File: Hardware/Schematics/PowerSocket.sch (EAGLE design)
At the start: 73 parts, among them T1 BT138-H, T2 BT138-H, T3 BT138-H, T4 BT138-H, T5 BT138-H, T6 BT138-H

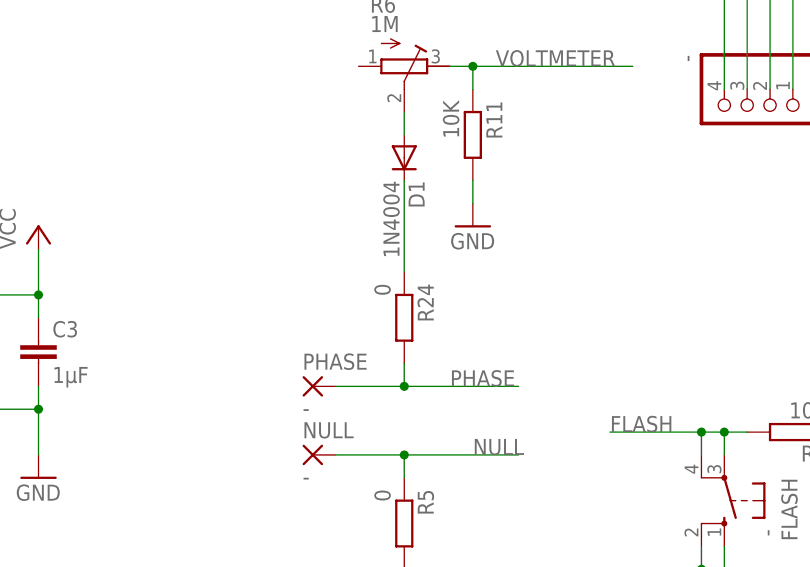
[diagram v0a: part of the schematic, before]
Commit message: Changed package for triac.
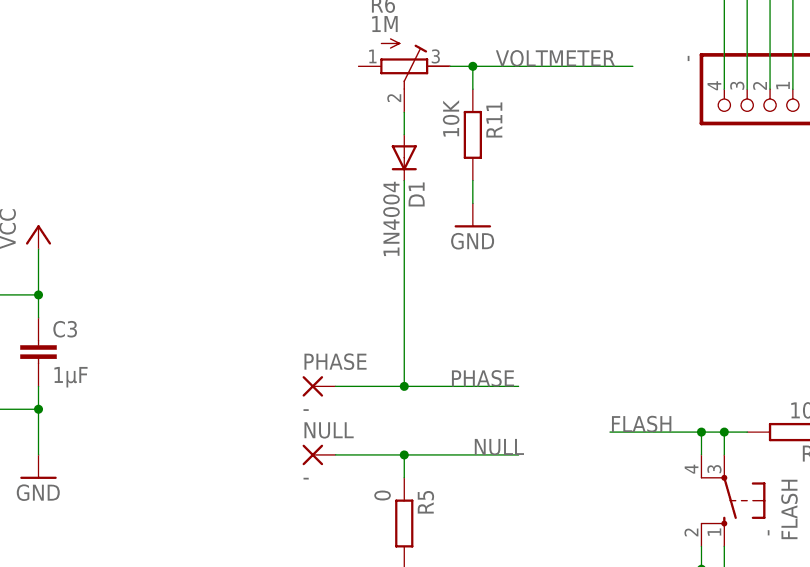
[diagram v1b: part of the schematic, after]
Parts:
- removed R24: 0, eagle-ltspice:RR2010
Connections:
- removed net N$41: D1.C, R24.1
- net PHASE: now also D1.C; no longer R24.2
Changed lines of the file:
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@@
 <grid distance="0.1" unitdist="inch" unit="inch" style="lines" multiple="1" display="no" altdistance="0.01" altunitdist="inch" altunit="inch"/>
 <layers>
-<layer number="1" name="Top" color="4" fill="1" visible="yes" active="no"/>
-<layer number="16" name="Bottom" color="1" fill="1" visible="yes" active="no"/>
-<layer number="17" name="Pads" color="2" fill="1" visible="yes" active="no"/>
-<layer number="18" name="Vias" color="2" fill="1" visible="yes" active="no"/>
-<layer number="19" name="Unrouted" color="6" fill="1" visible="yes" active="no"/>
-<layer number="20" name="Dimension" color="15" fill="1" visible="yes" active="no"/>
-<layer number="21" name="tPlace" color="7" fill="1" visible="yes" active="no"/>
-<layer number="22" name="bPlace" color="7" fill="1" visible="yes" active="no"/>
-<layer number="23" name="tOrigins" color="15" fill="1" visible="yes" active="no"/>
-<layer number="24" name="bOrigins" color="15" fill="1" visible="yes" active="no"/>
-<layer number="25" name="tNames" color="7" fill="1" visible="yes" active="no"/>
-<layer number="26" name="bNames" color="7" fill="1" visible="yes" active="no"/>
-<layer number="27" name="tValues" color="7" fill="1" visible="yes" active="no"/>
-<layer number="28" name="bValues" color="7" fill="1" visible="yes" active="no"/>
+<layer number="1" name="Top" color="4" fill="1" visible="no" active="no"/>
+<layer number="16" name="Bottom" color="1" fill="1" visible="no" active="no"/>
+<layer number="17" name="Pads" color="2" fill="1" visible="no" active="no"/>
+<layer number="18" name="Vias" color="2" fill="1" visible="no" active="no"/>
+<layer number="19" name="Unrouted" color="6" fill="1" visible="no" active="no"/>
+<layer number="20" name="Dimension" color="15" fill="1" visible="no" active="no"/>
+<layer number="21" name="tPlace" color="7" fill="1" visible="no" active="no"/>
+<layer number="22" name="bPlace" color="7" fill="1" visible="no" active="no"/>
+<layer number="23" name="tOrigins" color="15" fill="1" visible="no" active="no"/>
+<layer number="24" name="bOrigins" color="15" fill="1" visible="no" active="no"/>
+<layer number="25" name="tNames" color="7" fill="1" visible="no" active="no"/>
+<layer number="26" name="bNames" color="7" fill="1" visible="no" active="no"/>
+<layer number="27" name="tValues" color="7" fill="1" visible="no" active="no"/>
+<layer number="28" name="bValues" color="7" fill="1" visible="no" active="no"/>
 <layer number="29" name="tStop" color="7" fill="3" visible="no" active="no"/>
 <layer number="30" name="bStop" color="7" fill="6" visible="no" active="no"/>
@@
 <layer number="35" name="tGlue" color="7" fill="4" visible="no" active="no"/>
 <layer number="36" name="bGlue" color="7" fill="5" visible="no" active="no"/>
-<layer number="37" name="tTest" color="7" fill="1" visible="yes" active="no"/>
-<layer number="38" name="bTest" color="7" fill="1" visible="yes" active="no"/>
+<layer number="37" name="tTest" color="7" fill="1" visible="no" active="no"/>
+<layer number="38" name="bTest" color="7" fill="1" visible="no" active="no"/>
 <layer number="39" name="tKeepout" color="4" fill="11" visible="no" active="no"/>
 <layer number="40" name="bKeepout" color="1" fill="11" visible="no" active="no"/>
@@
 <layer number="44" name="Drills" color="7" fill="1" visible="no" active="no"/>
 <layer number="45" name="Holes" color="7" fill="1" visible="no" active="no"/>
-<layer number="46" name="Milling" color="3" fill="1" visible="yes" active="no"/>
-<layer number="47" name="Measures" color="7" fill="1" visible="yes" active="no"/>
-<layer number="48" name="Document" color="7" fill="1" visible="yes" active="no"/>
-<layer number="49" name="Reference" color="7" fill="1" visible="yes" active="no"/>
-<layer number="50" name="dxf" color="7" fill="1" visible="yes" active="no"/>
-<layer number="51" name="tDocu" color="7" fill="1" visible="yes" active="no"/>
-<layer number="52" name="bDocu" color="7" fill="1" visible="yes" active="no"/>
-<layer number="56" name="wert" color="7" fill="1" visible="yes" active="no"/>
+<layer number="46" name="Milling" color="3" fill="1" visible="no" active="no"/>
+<layer number="47" name="Measures" color="7" fill="1" visible="no" active="no"/>
+<layer number="48" name="Document" color="7" fill="1" visible="no" active="no"/>
+<layer number="49" name="Reference" color="7" fill="1" visible="no" active="no"/>
+<layer number="50" name="dxf" color="7" fill="1" visible="no" active="no"/>
+<layer number="51" name="tDocu" color="7" fill="1" visible="no" active="no"/>
+<layer number="52" name="bDocu" color="7" fill="1" visible="no" active="no"/>
+<layer number="56" name="wert" color="7" fill="1" visible="no" active="no"/>
 <layer number="90" name="Modules" color="5" fill="1" visible="yes" active="yes"/>
 <layer number="91" name="Nets" color="2" fill="1" visible="yes" active="yes"/>
@@
 <part name="R14" library="rcl" deviceset="R-EU_" device="R0805" value="150"/>
 <part name="R18" library="rcl" deviceset="R-EU_" device="R0805" value="150"/>
-<part name="R24" library="eagle-ltspice" deviceset="R" device="R2010" value="0"/>
 <part name="T1" library="triac" deviceset="BT138" device="-H"/>
 <part name="T2" library="triac" deviceset="BT138" device="-H"/>
@@
 <instance part="R14" gate="G$1" x="-152.4" y="144.78" rot="R90"/>
 <instance part="R18" gate="G$1" x="-152.4" y="55.88" rot="R270"/>
-<instance part="R24" gate="G$1" x="-35.56" y="-27.94" rot="R270"/>
 <instance part="T1" gate="G$1" x="-152.4" y="193.04" rot="R270"/>
 <instance part="T2" gate="G$1" x="-127" y="193.04" rot="R270"/>
@@
 <wire x1="-43.18" y1="-35.56" x2="-35.56" y2="-35.56" width="0.1524" layer="91"/>
 <label x="-30.48" y="-35.56" size="1.778" layer="95"/>
-<pinref part="R24" gate="G$1" pin="2"/>
 <wire x1="-35.56" y1="-35.56" x2="-22.86" y2="-35.56" width="0.1524" layer="91"/>
-<wire x1="-35.56" y1="-35.56" x2="-35.56" y2="-33.02" width="0.1524" layer="91"/>
 <junction x="-35.56" y="-35.56"/>
+<pinref part="D1" gate="1" pin="C"/>
+<wire x1="-35.56" y1="-35.56" x2="-35.56" y2="-12.7" width="0.1524" layer="91"/>
 </segment>
 <segment>
@@
 </segment>
 </net>
-<net name="N$41" class="0">
-<segment>
-<pinref part="R24" gate="G$1" pin="1"/>
-<pinref part="D1" gate="1" pin="C"/>
-<wire x1="-35.56" y1="-22.86" x2="-35.56" y2="-12.7" width="0.1524" layer="91"/>
-</segment>
-</net>

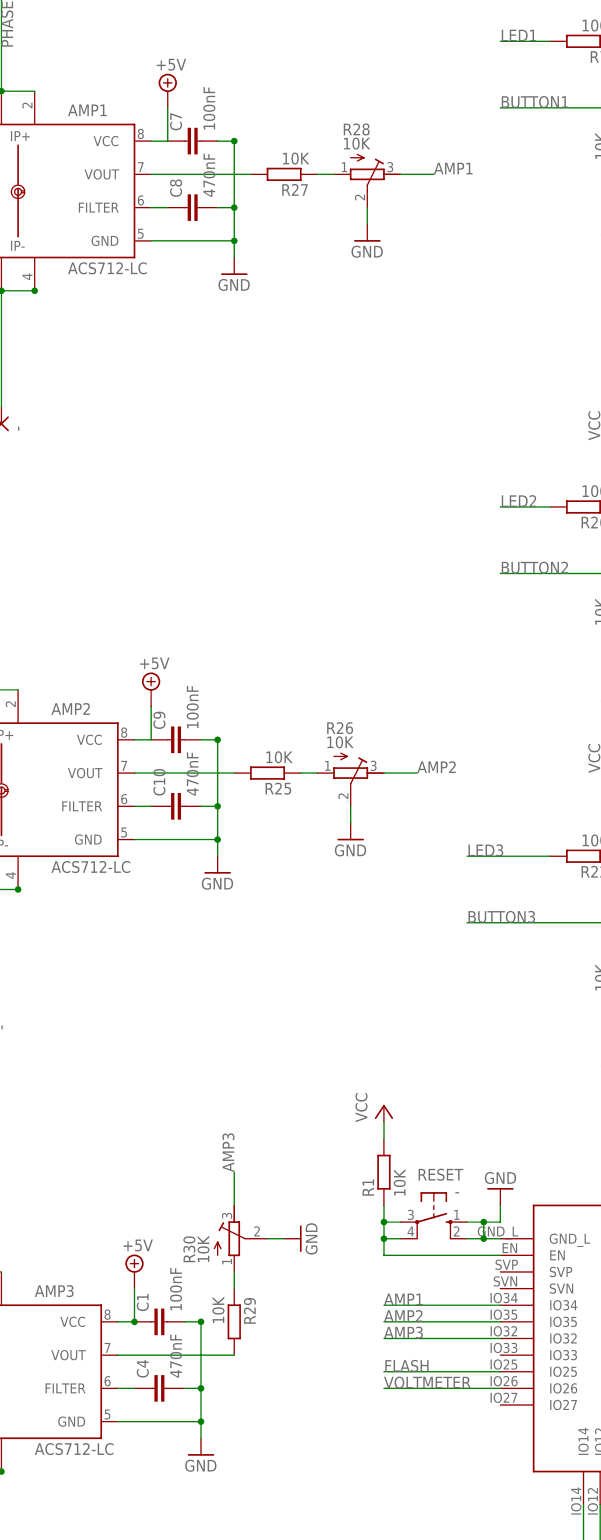
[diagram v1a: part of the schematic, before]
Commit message: Fixed error in wiring of voltage divider.
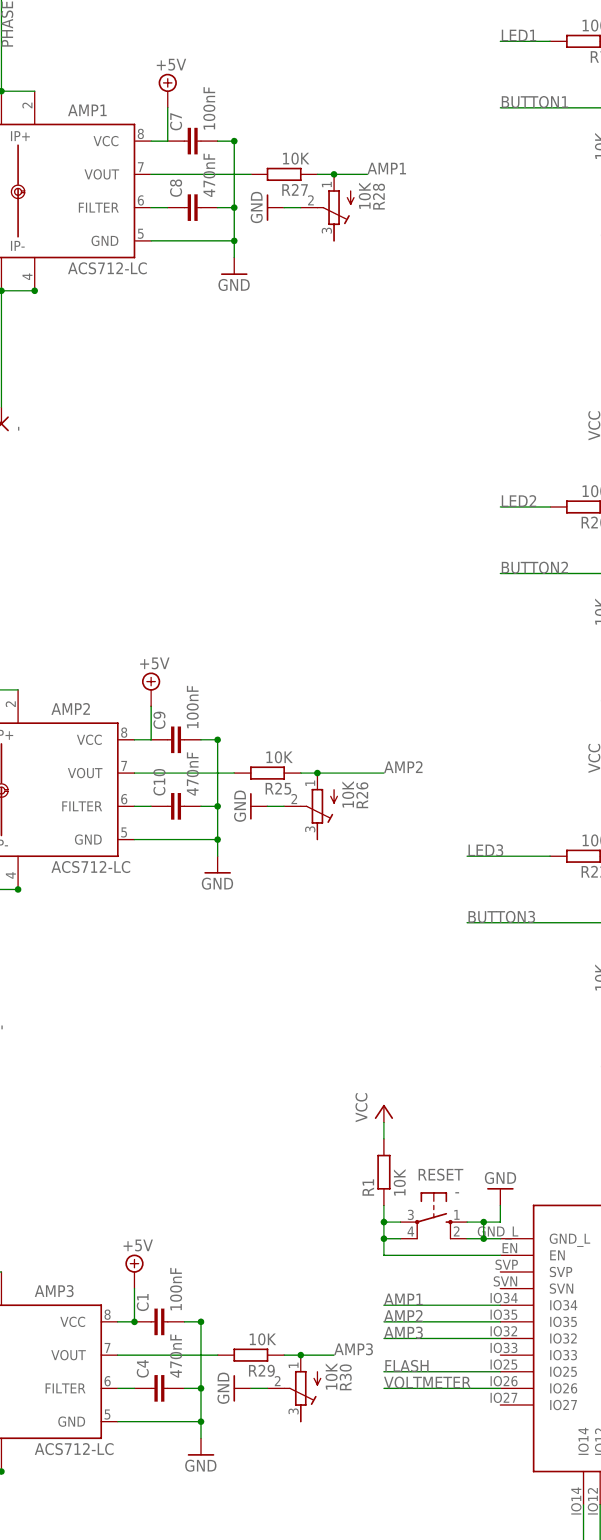
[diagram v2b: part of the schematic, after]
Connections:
- removed net N$38: R25.1, R26.A
- removed net N$39 (its old number): R27.1, R28.A
- removed net N$40: R29.1, R30.A
- net AMP1: now also R27.1, R28.A; no longer R28.E
- net AMP2: now also R25.1, R26.A; no longer R26.E
- net AMP3: now also R29.1, R30.A; no longer R30.E
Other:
- moved on the sheet: R26, R28, R29, R30
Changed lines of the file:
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@@
 <instance part="C4" gate="G$1" x="-66.04" y="33.02" rot="R90"/>
 <instance part="R25" gate="G$1" x="-48.26" y="127" rot="R180"/>
-<instance part="R26" gate="G$1" x="-35.56" y="127" rot="R270"/>
-<instance part="GND11" gate="1" x="-35.56" y="116.84"/>
+<instance part="R26" gate="G$1" x="-40.64" y="121.92" rot="R180"/>
+<instance part="GND11" gate="1" x="-50.8" y="121.92" rot="R270"/>
 <instance part="R27" gate="G$1" x="-45.72" y="218.44" rot="R180"/>
-<instance part="R28" gate="G$1" x="-33.02" y="218.44" rot="R270"/>
-<instance part="GND12" gate="1" x="-33.02" y="208.28"/>
-<instance part="R29" gate="G$1" x="-53.34" y="43.18" rot="R270"/>
-<instance part="R30" gate="G$1" x="-53.34" y="55.88"/>
-<instance part="GND13" gate="1" x="-43.18" y="55.88" rot="R90"/>
+<instance part="R28" gate="G$1" x="-38.1" y="213.36" rot="R180"/>
+<instance part="GND12" gate="1" x="-48.26" y="213.36" rot="R270"/>
+<instance part="R29" gate="G$1" x="-50.8" y="38.1" rot="R180"/>
+<instance part="R30" gate="G$1" x="-43.18" y="33.02" rot="R180"/>
+<instance part="GND13" gate="1" x="-53.34" y="33.02" rot="R270"/>
 <instance part="U$1" gate="G$1" x="68.58" y="-53.34"/>
 <instance part="GND16" gate="1" x="45.72" y="-55.88" rot="R270"/>
@@
 </segment>
 <segment>
-<pinref part="R26" gate="G$1" pin="S"/>
-<pinref part="GND11" gate="1" pin="GND"/>
-<wire x1="-35.56" y1="121.92" x2="-35.56" y2="119.38" width="0.1524" layer="91"/>
-</segment>
-<segment>
-<pinref part="R28" gate="G$1" pin="S"/>
-<pinref part="GND12" gate="1" pin="GND"/>
-<wire x1="-33.02" y1="213.36" x2="-33.02" y2="210.82" width="0.1524" layer="91"/>
-</segment>
-<segment>
-<pinref part="R30" gate="G$1" pin="S"/>
-<pinref part="GND13" gate="1" pin="GND"/>
-<wire x1="-48.26" y1="55.88" x2="-45.72" y2="55.88" width="0.1524" layer="91"/>
-</segment>
-<segment>
 <pinref part="U$1" gate="G$1" pin="IN-"/>
 <pinref part="GND16" gate="1" pin="GND"/>
@@
 <junction x="86.36" y="-48.26"/>
 <junction x="86.36" y="-50.8"/>
+</segment>
+<segment>
+<pinref part="R30" gate="G$1" pin="S"/>
+<pinref part="GND13" gate="1" pin="GND"/>
+<wire x1="-48.26" y1="33.02" x2="-50.8" y2="33.02" width="0.1524" layer="91"/>
+</segment>
+<segment>
+<pinref part="R26" gate="G$1" pin="S"/>
+<pinref part="GND11" gate="1" pin="GND"/>
+<wire x1="-45.72" y1="121.92" x2="-48.26" y2="121.92" width="0.1524" layer="91"/>
+</segment>
+<segment>
+<pinref part="R28" gate="G$1" pin="S"/>
+<pinref part="GND12" gate="1" pin="GND"/>
+<wire x1="-43.18" y1="213.36" x2="-45.72" y2="213.36" width="0.1524" layer="91"/>
 </segment>
 </net>
@@
 </segment>
 <segment>
-<pinref part="R30" gate="G$1" pin="E"/>
-<wire x1="-53.34" y1="60.96" x2="-53.34" y2="66.04" width="0.1524" layer="91"/>
-<label x="-53.34" y="66.04" size="1.778" layer="95" rot="R90"/>
+<pinref part="R29" gate="G$1" pin="1"/>
+<pinref part="R30" gate="G$1" pin="A"/>
+<wire x1="-45.72" y1="38.1" x2="-43.18" y2="38.1" width="0.1524" layer="91"/>
+<wire x1="-43.18" y1="38.1" x2="-38.1" y2="38.1" width="0.1524" layer="91"/>
+<junction x="-43.18" y="38.1"/>
+<label x="-38.1" y="38.1" size="1.778" layer="95"/>
 </segment>
 </net>
@@
 </segment>
 <segment>
-<pinref part="R26" gate="G$1" pin="E"/>
-<wire x1="-30.48" y1="127" x2="-25.4" y2="127" width="0.1524" layer="91"/>
-<label x="-25.4" y="127" size="1.778" layer="95"/>
+<pinref part="R25" gate="G$1" pin="1"/>
+<pinref part="R26" gate="G$1" pin="A"/>
+<wire x1="-43.18" y1="127" x2="-40.64" y2="127" width="0.1524" layer="91"/>
+<wire x1="-40.64" y1="127" x2="-30.48" y2="127" width="0.1524" layer="91"/>
+<junction x="-40.64" y="127"/>
+<label x="-30.48" y="127" size="1.778" layer="95"/>
 </segment>
 </net>
@@
 </segment>
 <segment>
-<pinref part="R28" gate="G$1" pin="E"/>
-<wire x1="-27.94" y1="218.44" x2="-22.86" y2="218.44" width="0.1524" layer="91"/>
-<label x="-22.86" y="218.44" size="1.778" layer="95"/>
+<pinref part="R27" gate="G$1" pin="1"/>
+<pinref part="R28" gate="G$1" pin="A"/>
+<wire x1="-40.64" y1="218.44" x2="-38.1" y2="218.44" width="0.1524" layer="91"/>
+<wire x1="-38.1" y1="218.44" x2="-33.02" y2="218.44" width="0.1524" layer="91"/>
+<junction x="-38.1" y="218.44"/>
+<label x="-33.02" y="218.44" size="1.778" layer="95"/>
 </segment>
 </net>
@@
 </segment>
 </net>
-<net name="N$37" class="0">
-<segment>
-<pinref part="AMP2" gate="G$1" pin="VOUT"/>
-<pinref part="R25" gate="G$1" pin="2"/>
-<wire x1="-68.58" y1="127" x2="-53.34" y2="127" width="0.1524" layer="91"/>
-</segment>
-</net>
-<net name="N$38" class="0">
-<segment>
-<pinref part="R25" gate="G$1" pin="1"/>
-<pinref part="R26" gate="G$1" pin="A"/>
-<wire x1="-40.64" y1="127" x2="-43.18" y2="127" width="0.1524" layer="91"/>
-</segment>
-</net>
-<net name="N$39" class="0">
-<segment>
-<pinref part="R27" gate="G$1" pin="1"/>
-<pinref part="R28" gate="G$1" pin="A"/>
-<wire x1="-38.1" y1="218.44" x2="-40.64" y2="218.44" width="0.1524" layer="91"/>
-</segment>
-</net>
-<net name="N$40" class="0">
-<segment>
-<pinref part="R29" gate="G$1" pin="1"/>
-<pinref part="R30" gate="G$1" pin="A"/>
-<wire x1="-53.34" y1="50.8" x2="-53.34" y2="48.26" width="0.1524" layer="91"/>
-</segment>
-</net>
-<net name="N$43" class="0">
-<segment>
-<pinref part="AMP3" gate="G$1" pin="VOUT"/>
-<pinref part="R29" gate="G$1" pin="2"/>
-<wire x1="-71.12" y1="38.1" x2="-53.34" y2="38.1" width="0.1524" layer="91"/>
-</segment>
-</net>
 <net name="+5V" class="0">
 <segment>
@@
 </segment>
 </net>
-<net name="N$44" class="0">
+<net name="N$37" class="0">
+<segment>
+<pinref part="AMP3" gate="G$1" pin="VOUT"/>
+<pinref part="R29" gate="G$1" pin="2"/>
+<wire x1="-71.12" y1="38.1" x2="-55.88" y2="38.1" width="0.1524" layer="91"/>
+</segment>
+</net>
+<net name="N$39" class="0">
+<segment>
+<pinref part="AMP2" gate="G$1" pin="VOUT"/>
+<pinref part="R25" gate="G$1" pin="2"/>
+<wire x1="-68.58" y1="127" x2="-53.34" y2="127" width="0.1524" layer="91"/>
+</segment>
+</net>
+<net name="N$41" class="0">
 <segment>
 <pinref part="AMP1" gate="G$1" pin="VOUT"/>

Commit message: Fixed triac wiring.
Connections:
- removed net N$14: NULL2-OUT.P, R13.2, T4.A2
- new net NULL_: NULL3-OUT.P, T6.A1
- net N$17: now also NULL2-OUT.P, T4.A1; no longer NULL1-OUT.P, R4.2, T2.A2
- net N$8: now also NULL1-OUT.P, T2.A1; no longer NULL3-OUT.P, R17.2, T6.A2
- net NULL: now also R13.2, R17.2, R4.2, T2.A2, T4.A2, T6.A2; no longer T2.A1, T4.A1, T6.A1
- net PHASE: now also R10.2, R15.2, R19.2, T1.A2, T3.A2, T5.A2; no longer T1.A1, T3.A1, T5.A1
- net PHASE1: now also T1.A1; no longer R10.2, T1.A2
- net PHASE2: now also T3.A1; no longer R15.2, T3.A2
- net PHASE3: now also T5.A1; no longer R19.2, T5.A2
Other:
- moved on the sheet: NULL1-OUT, NULL2-OUT, NULL3-OUT

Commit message: Changed resistor values.
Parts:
- R10, R13, R15, R17, R19, R4: value 150 -> 300
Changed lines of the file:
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@@
 <part name="OK1" library="optocoupler" deviceset="MOC30*" device="S" technology="41" value="MOC3041S"/>
 <part name="P+6" library="supply1" deviceset="VCC" device=""/>
-<part name="R4" library="eagle-ltspice" deviceset="R" device="R2010" value="150"/>
+<part name="R4" library="eagle-ltspice" deviceset="R" device="R2010" value="300"/>
 <part name="R9" library="rcl" deviceset="R-EU_" device="R0805" value="150"/>
 <part name="OK2" library="optocoupler" deviceset="MOC30*" device="S" technology="41" value="MOC3041S"/>
 <part name="P+10" library="supply1" deviceset="VCC" device=""/>
-<part name="R10" library="eagle-ltspice" deviceset="R" device="R2010" value="150"/>
+<part name="R10" library="eagle-ltspice" deviceset="R" device="R2010" value="300"/>
 <part name="GND1" library="supply1" deviceset="GND" device=""/>
 <part name="R5" library="eagle-ltspice" deviceset="R" device="R2010" value="0"/>
@@
 <part name="OK4" library="optocoupler" deviceset="MOC30*" device="S" technology="41" value="MOC3041S"/>
 <part name="P+12" library="supply1" deviceset="VCC" device=""/>
-<part name="R13" library="eagle-ltspice" deviceset="R" device="R2010" value="150"/>
+<part name="R13" library="eagle-ltspice" deviceset="R" device="R2010" value="300"/>
 <part name="OK3" library="optocoupler" deviceset="MOC30*" device="S" technology="41" value="MOC3041S"/>
 <part name="P+13" library="supply1" deviceset="VCC" device=""/>
-<part name="R15" library="eagle-ltspice" deviceset="R" device="R2010" value="150"/>
+<part name="R15" library="eagle-ltspice" deviceset="R" device="R2010" value="300"/>
 <part name="NULL3-OUT" library="wirepad" deviceset="3,81/1,4" device="" value="-"/>
 <part name="R16" library="rcl" deviceset="R-EU_" device="R0805" value="150"/>
 <part name="OK5" library="optocoupler" deviceset="MOC30*" device="S" technology="41" value="MOC3041S"/>
 <part name="P+15" library="supply1" deviceset="VCC" device=""/>
-<part name="R17" library="eagle-ltspice" deviceset="R" device="R2010" value="150"/>
+<part name="R17" library="eagle-ltspice" deviceset="R" device="R2010" value="300"/>
 <part name="OK6" library="optocoupler" deviceset="MOC30*" device="S" technology="41" value="MOC3041S"/>
 <part name="P+16" library="supply1" deviceset="VCC" device=""/>
-<part name="R19" library="eagle-ltspice" deviceset="R" device="R2010" value="150"/>
+<part name="R19" library="eagle-ltspice" deviceset="R" device="R2010" value="300"/>
 <part name="R20" library="rcl" deviceset="R-EU_" device="R0805" value="100"/>
 <part name="P+17" library="supply1" deviceset="VCC" device=""/>
